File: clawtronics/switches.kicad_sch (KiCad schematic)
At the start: 9 parts, among them J6 Screw_Terminal_01x09, J7 Screw_Terminal_01x15, J8 Screw_Terminal_01x02, Q1 AO3400A

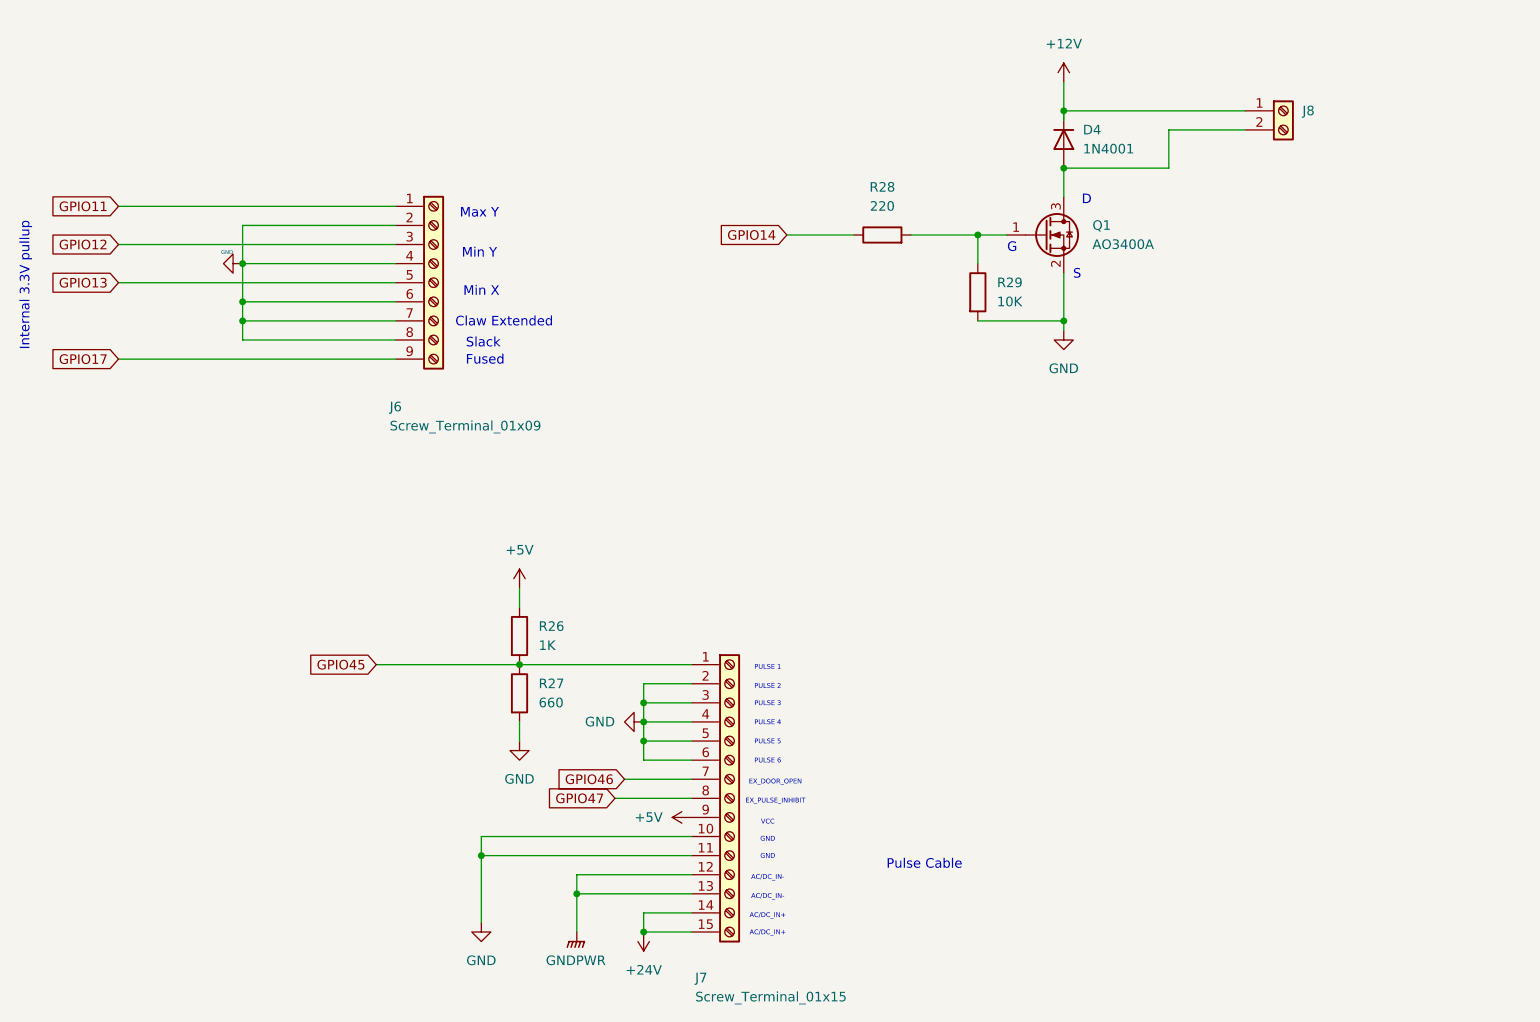
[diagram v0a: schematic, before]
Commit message: layout with hierarchical sheets
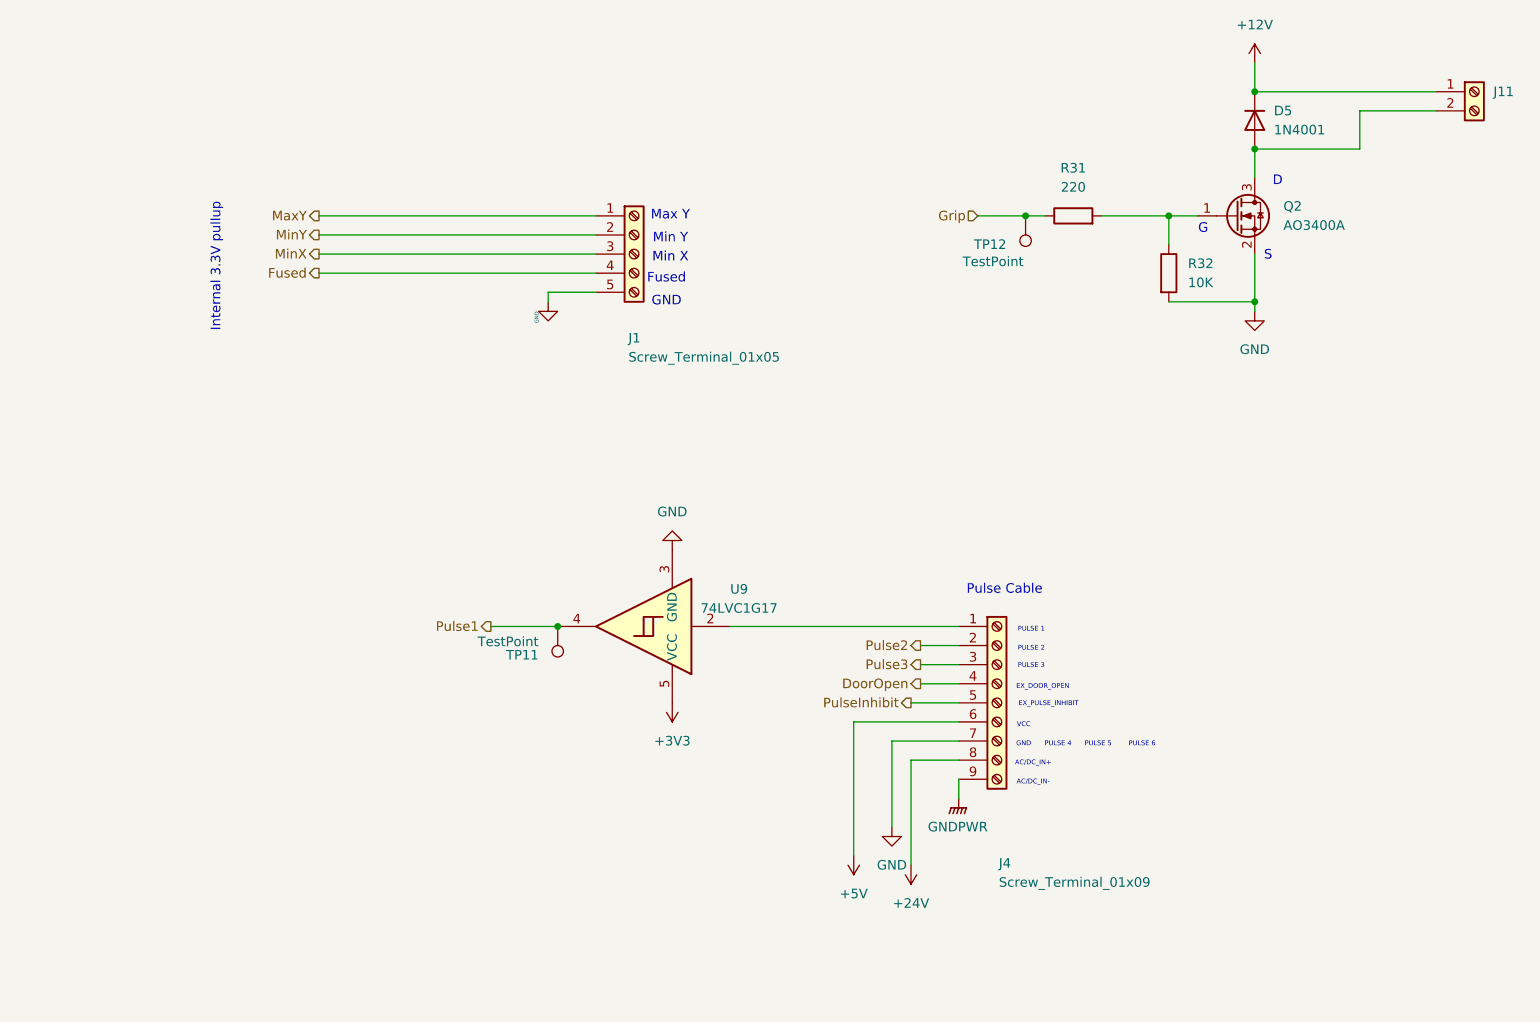
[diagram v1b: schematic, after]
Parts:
- removed D4: 1N4001, Diode_THT:D_DO-41_SOD81_P10.16mm_Horizontal, symbol Diode:1N4001
- removed J6: Screw_Terminal_01x09, TerminalBlock:TerminalBlock_MaiXu_MX126-5.0-09P_1x09_P5.00mm, symbol Connector:Screw_Terminal_01x09
- removed J7: Screw_Terminal_01x15, TerminalBlock:TerminalBlock_MaiXu_MX126-5.0-15P_1x15_P5.00mm, symbol Connector:Screw_Terminal_01x15
- removed J8: Screw_Terminal_01x02, TerminalBlock:TerminalBlock_MaiXu_MX126-5.0-02P_1x02_P5.00mm, symbol Connector:Screw_Terminal_01x02
- removed Q1: AO3400A, Package_TO_SOT_SMD:SOT-23, symbol Transistor_FET:AO3400A
- removed R26: 1K, Resistor_SMD:R_0603_1608Metric, symbol Device:R
- removed R27: 660, Resistor_SMD:R_0603_1608Metric, symbol Device:R
- removed R28: 220, Resistor_SMD:R_0603_1608Metric, symbol Device:R
- removed R29: 10K, Resistor_SMD:R_0603_1608Metric, symbol Device:R
- added D5: 1N4001, Diode_THT:D_DO-41_SOD81_P10.16mm_Horizontal, symbol Diode:1N4001
- added J1: Screw_Terminal_01x05, TerminalBlock_Phoenix:TerminalBlock_Phoenix_MKDS-1,5-5_1x05_P5.00mm_Horizontal, symbol Connector:Screw_Terminal_01x05
- added J11: Screw_Terminal_01x02, TerminalBlock_Phoenix:TerminalBlock_Phoenix_MKDS-1,5-2_1x02_P5.00mm_Horizontal, symbol Connector:Screw_Terminal_01x02
- added J4: Screw_Terminal_01x09, TerminalBlock_Phoenix:TerminalBlock_Phoenix_MKDS-1,5-9_1x09_P5.00mm_Horizontal, symbol Connector:Screw_Terminal_01x09
- added Q2: AO3400A, Package_TO_SOT_SMD:SOT-23, symbol Transistor_FET:AO3400A
- added R31: 220, Resistor_SMD:R_0603_1608Metric, symbol Device:R
- added R32: 10K, Resistor_SMD:R_0603_1608Metric, symbol Device:R
- added TP11, TP12: TestPoint, TestPoint:TestPoint_Pad_1.0x1.0mm, symbol Connector:TestPoint
- added U9: 74LVC1G17, Package_SON:Texas_X2SON-5_0.8x0.8mm_P0.48mm, symbol 74xGxx:74LVC1G17
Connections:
- net +12V: now also D5.1 (K), J11.1 (Pin_1)
- net +24V: now also J4.8 (Pin_8)
- net +5V: now also J4.6 (Pin_6)
- net GND: now also J1.5 (Pin_5), J4.7 (Pin_7), Q2.2 (S), R32.2, U9.3 (GND)
- net GNDPWR: now also J4.9 (Pin_9)
- new net: J4.1 (Pin_1), U9.2
- new net: D5.2 (A), J11.2 (Pin_2), Q2.3 (D)
- new net: Q2.1 (G), R31.2, R32.1
- new net +3V3: U9.5 (VCC)
- new net DoorOpen: J4.4 (Pin_4)
- new net Fused: J1.4 (Pin_4)
- new net Grip: R31.1, TP12.1
- new net MaxY: J1.1 (Pin_1)
- new net MinX: J1.3 (Pin_3)
- new net MinY: J1.2 (Pin_2)
- new net Pulse1: TP11.1, U9.4
- new net Pulse2: J4.2 (Pin_2)
- new net Pulse3: J4.3 (Pin_3)
- new net PulseInhibit: J4.5 (Pin_5)
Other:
- note removed: "Claw Extended"
- note removed: "Slack"

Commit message: finished layout
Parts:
- U9: footprint Package_SON:Texas_X2SON-5_0.8x0.8mm_P0.48mm -> Package_SON:Texas_X2SON-5_0.8x0.8mm_P0.48mm_RoutingVia
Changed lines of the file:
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@@
 			)
 		)
-		(property "Footprint" "Package_SON:Texas_X2SON-5_0.8x0.8mm_P0.48mm"
+		(property "Footprint" "Package_SON:Texas_X2SON-5_0.8x0.8mm_P0.48mm_RoutingVia"
 			(at 109.22 109.22 0)
 			(hide yes)

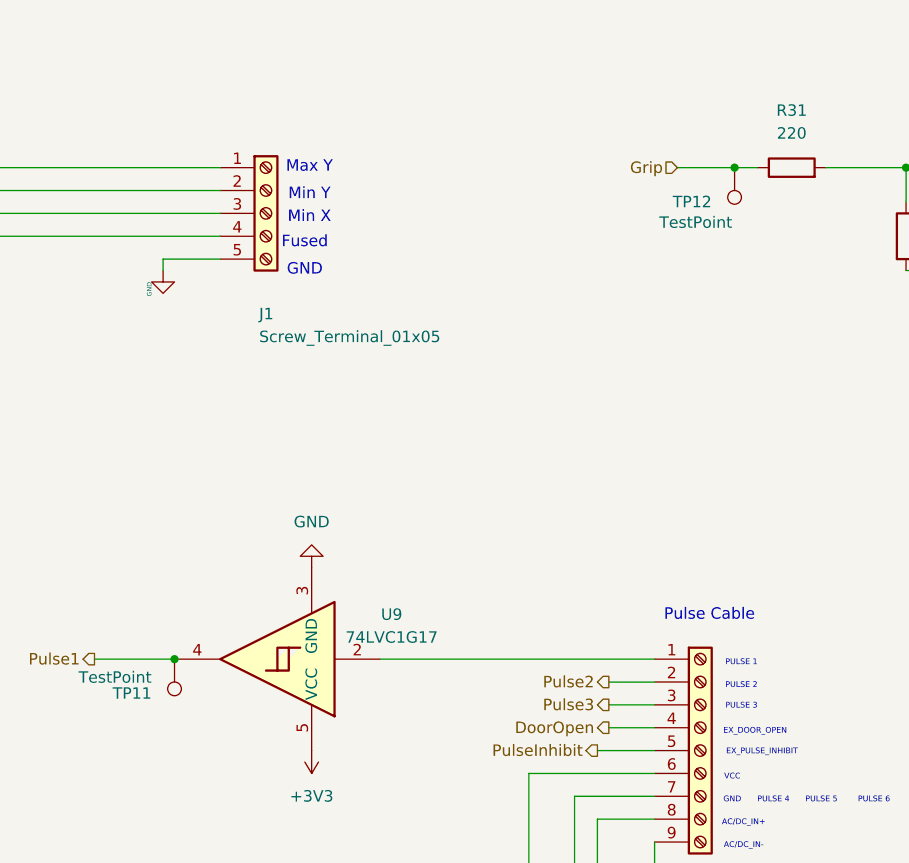
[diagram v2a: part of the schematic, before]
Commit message: update BOM with PNs
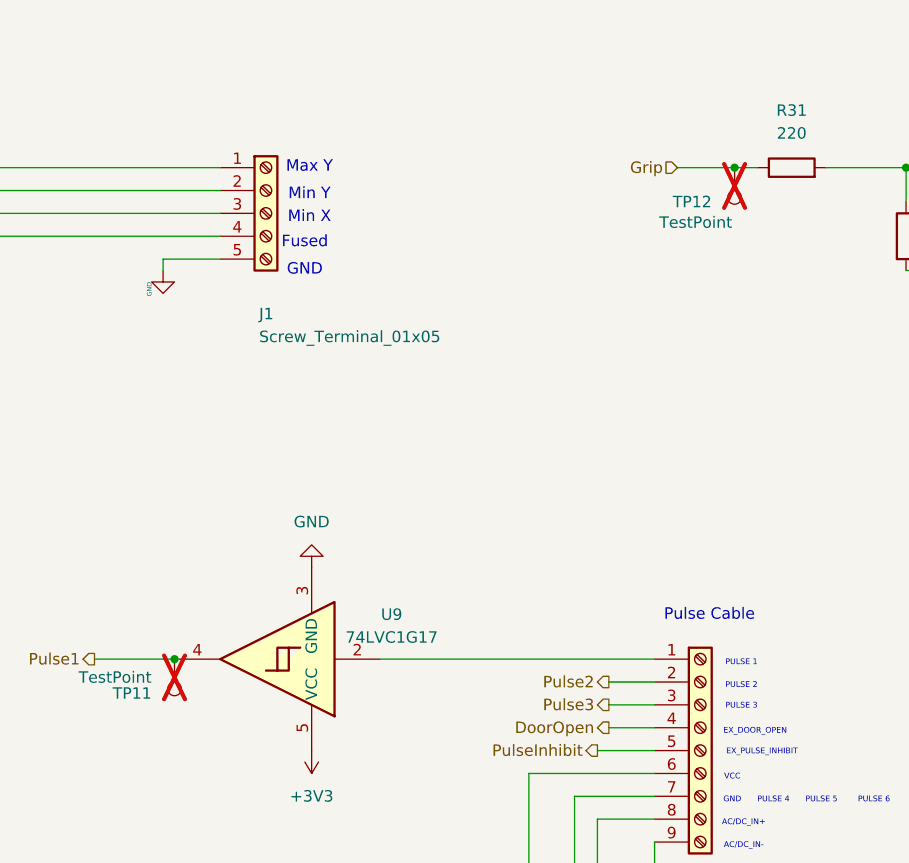
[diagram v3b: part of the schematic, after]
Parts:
- D5: Part Number (none) -> 1N4001
- J1: Part Number (none) -> 1869091
- J11: Part Number (none) -> 1729128
- J4: Part Number (none) -> Put 5 + 4 together
- Q2: Part Number (none) -> AO3400A
- R31: Part Number (none) -> RMCF0603JT220R
- R32: Part Number (none) -> RC0603FR-0710KL
- TP11, TP12: now not fitted
- U9: Part Number (none) -> 74LVC1G17
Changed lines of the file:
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@@
+			)
+		)
+		(property "Part Number" "74LVC1G17"
+			(at 106.68 109.22 0)
+			(hide yes)
+			(show_name no)
+			(do_not_autoplace no)
+			(effects
+				(font
+					(size 1.27 1.27)
+				)
 			)
 		)
@@
 			)
 		)
+		(property "Part Number" "1869091"
+			(at 106.68 59.69 0)
+			(hide yes)
+			(show_name no)
+			(do_not_autoplace no)
+			(effects
+				(font
+					(size 1.27 1.27)
+				)
+			)
+		)
 		(pin "3"
 		)
@@
 			)
 		)
+		(property "Part Number" "1N4001"
+			(at 189.23 41.91 90)
+			(hide yes)
+			(show_name no)
+			(do_not_autoplace no)
+			(effects
+				(font
+					(size 1.27 1.27)
+				)
+			)
+		)
 		(pin "1"
 		)
@@
 			)
 		)
+		(property "Part Number" "1729128"
+			(at 218.44 38.1 0)
+			(hide yes)
+			(show_name no)
+			(do_not_autoplace no)
+			(effects
+				(font
+					(size 1.27 1.27)
+				)
+			)
+		)
 		(pin "2"
 		)
@@
 			)
 		)
+		(property "Part Number" "Put 5 + 4 together"
+			(at 154.94 119.38 0)
+			(hide yes)
+			(show_name no)
+			(do_not_autoplace no)
+			(effects
+				(font
+					(size 1.27 1.27)
+				)
+			)
+		)
 		(pin "9"
 		)
@@
 			)
 		)
+		(property "Part Number" "RMCF0603JT220R"
+			(at 165.1 54.61 90)
+			(hide yes)
+			(show_name no)
+			(do_not_autoplace no)
+			(effects
+				(font
+					(size 1.27 1.27)
+				)
+			)
+		)
 		(pin "2"
 		)
@@
 		(on_board yes)
 		(in_pos_files yes)
-		(dnp no)
+		(dnp yes)
 		(property "Reference" "TP12"
 			(at 156.21 58.42 0)
@@
 		)
 		(property "Description" "test point"
+			(at 158.75 54.61 0)
+			(hide yes)
+			(show_name no)
+			(do_not_autoplace no)
+			(effects
+				(font
+					(size 1.27 1.27)
+				)
+			)
+		)
+		(property "Part Number" ""
 			(at 158.75 54.61 0)
 			(hide yes)
@@
 			)
 		)
+		(property "Part Number" "AO3400A"
+			(at 186.69 54.61 0)
+			(hide yes)
+			(show_name no)
+			(do_not_autoplace no)
+			(effects
+				(font
+					(size 1.27 1.27)
+				)
+			)
+		)
 		(pin "2"
 		)
@@
 		(on_board yes)
 		(in_pos_files yes)
-		(dnp no)
+		(dnp yes)
 		(property "Reference" "TP11"
 			(at 93.98 113.03 0)
@@
 		)
 		(property "Description" "test point"
+			(at 96.52 109.22 0)
+			(hide yes)
+			(show_name no)
+			(do_not_autoplace no)
+			(effects
+				(font
+					(size 1.27 1.27)
+				)
+			)
+		)
+		(property "Part Number" ""
 			(at 96.52 109.22 0)
 			(hide yes)
@@
 			(at 177.8 62.23 0)
 			(hide yes)
+			(show_name no)
+			(do_not_autoplace no)
+			(effects
+				(font
+					(size 1.27 1.27)
+				)
+			)
+		)
+		(property "Part Number" "RC0603FR-0710KL"
+			(at 177.8 62.23 0)
+			(hide yes)
